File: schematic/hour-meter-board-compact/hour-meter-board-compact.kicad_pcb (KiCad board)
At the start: 2 copper layers, 80 x 70 mm, 115 parts, among them J101 VIN 9-36V, J102 PSU header, J201 USB-C, J301 VEHICLE IN, J501 WP, J701 RS485, J702 TERM, J703 BIAS, J801 UART, J802 GPS, J803 QWIIC, J804 EXP, Q201 MMBT3904, Q202 MMBT3904, SW201 RESET, SW202 BOOT, U201 ESP32-WROOM-32E-N4, U202 CH340C, U203 USBLC6-2SC6, U204 AMS1117-3.3, U301 PC817C-S, U302 PC817C-S, U401 DS3231MZ+TRL, U501 AT24C256 DIP-8 (socketed), U601 MPU-6500, U602 LIS3MDLTR, U701 THVD2410DR, U801 74LVC1G17GW, U802 SRV05-4

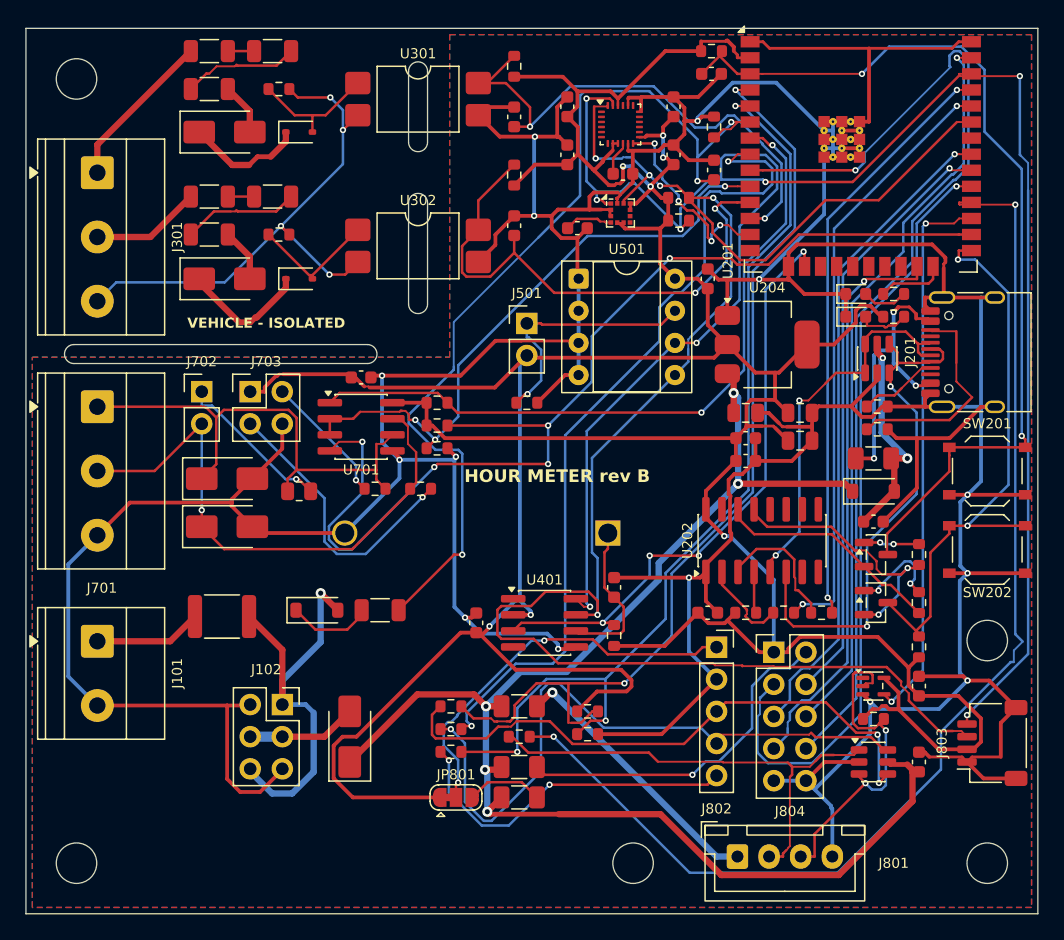
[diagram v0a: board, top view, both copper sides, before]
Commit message: fix(pcb): finish compact board routing and refresh JLCPCB order files
- Take the board tidied by hand in KiCad 10 (routing/finish-best) into the
  main board file
- Keep 2 copper layers: importing the KiCad 5 JLCPCB_1-2Layer template had
  enabled empty In1/In2 layers, a 4-layer stackup and "Front"/"Back" layer
  names, which turned the Gerbers into a 4-layer order
- Restore the Vehicle (0.8 mm), Power and Plane net classes the import
  removed; put back the 0.8 mm routes of R302-R303 and R307-R308 and refill
  the pours, which had come within 0.2-0.6 mm of vehicle-voltage copper
- Keep the template's rules (0.127 mm clearance, 0.12 mm mask web), all
  within JLCPCB's current limits
- Regenerate the Gerber zip, BOM and CPL (C602 and C605 rotated) and record
  the checks in the README
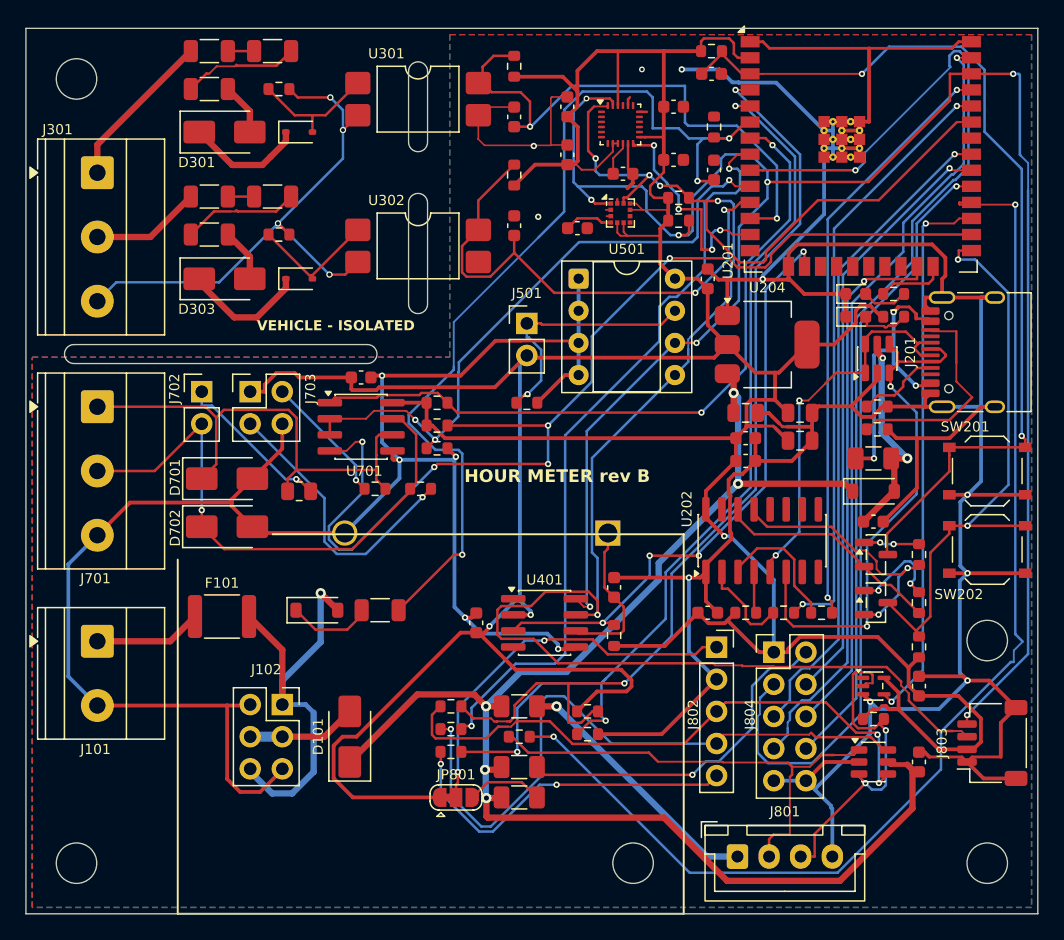
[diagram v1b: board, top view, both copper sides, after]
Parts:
- moved C605 0.40 mm to (151.2, 110.4), turned to 0 degrees
- turned C602 to 0 degrees
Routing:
- net GND: track 523.1 -> 472.6 mm, vias 14 -> 15
- net +3V3: track 325.5 -> 331.6 mm, vias 7 -> 3
- net /GPS_RXD: track 65.5 -> 60.1 mm
- net /IMU_INT: track 15.8 -> 18.0 mm
- net /ALT_IN_N: track 41.7 -> 43.5 mm
- net /I2C_SDA: track 141.4 -> 143.0 mm
- net /Ports (UART, GPS, Qwiic, expansion)/UART_5V: track 21.7 -> 20.8 mm
- net Net-(J201-CC1): track 6.30 -> 7.21 mm
- net /PULSE_IN_N: track 43.3 -> 42.4 mm
- net /RS485_DE: track 48.7 -> 49.5 mm
- net /Ports (UART, GPS, Qwiic, expansion)/GPS_PPS_EXT: track 27.4 -> 28.2 mm
- net /Ports (UART, GPS, Qwiic, expansion)/GPS_VCC: track 31.4 -> 30.6 mm
- net /GPS_PPS: track 76.4 -> 77.1 mm
- net /ESP32 core + USB (DevKitC)/USB_DM: track 41.1 -> 41.7 mm
- net +5V: track 117.3 -> 117.8 mm
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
